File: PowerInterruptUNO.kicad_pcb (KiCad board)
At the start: 2 copper layers, 68.6 x 53.3 mm, 8 parts, among them J1 Power, J2 Digital/PWM, J3 Analog, J4 Digital/PWM

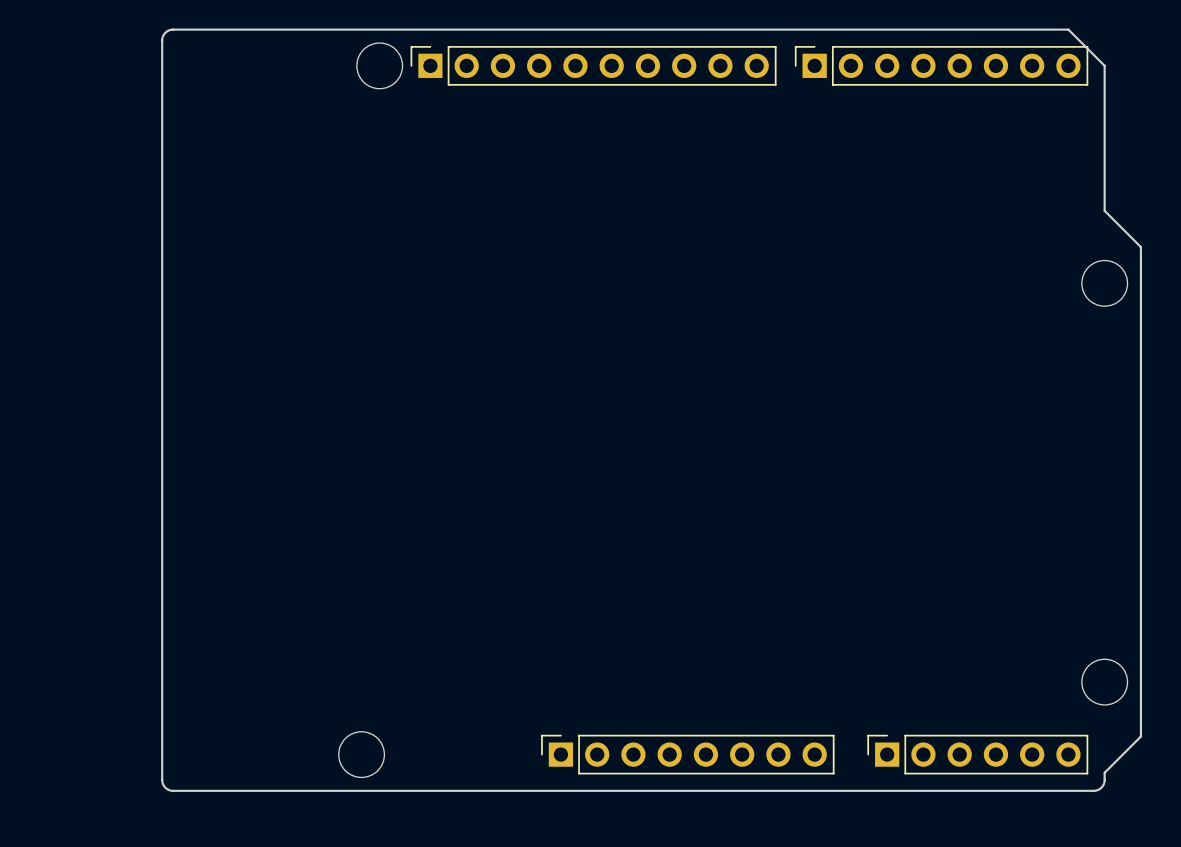
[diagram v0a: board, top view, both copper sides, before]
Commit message: Place parts on PCB.
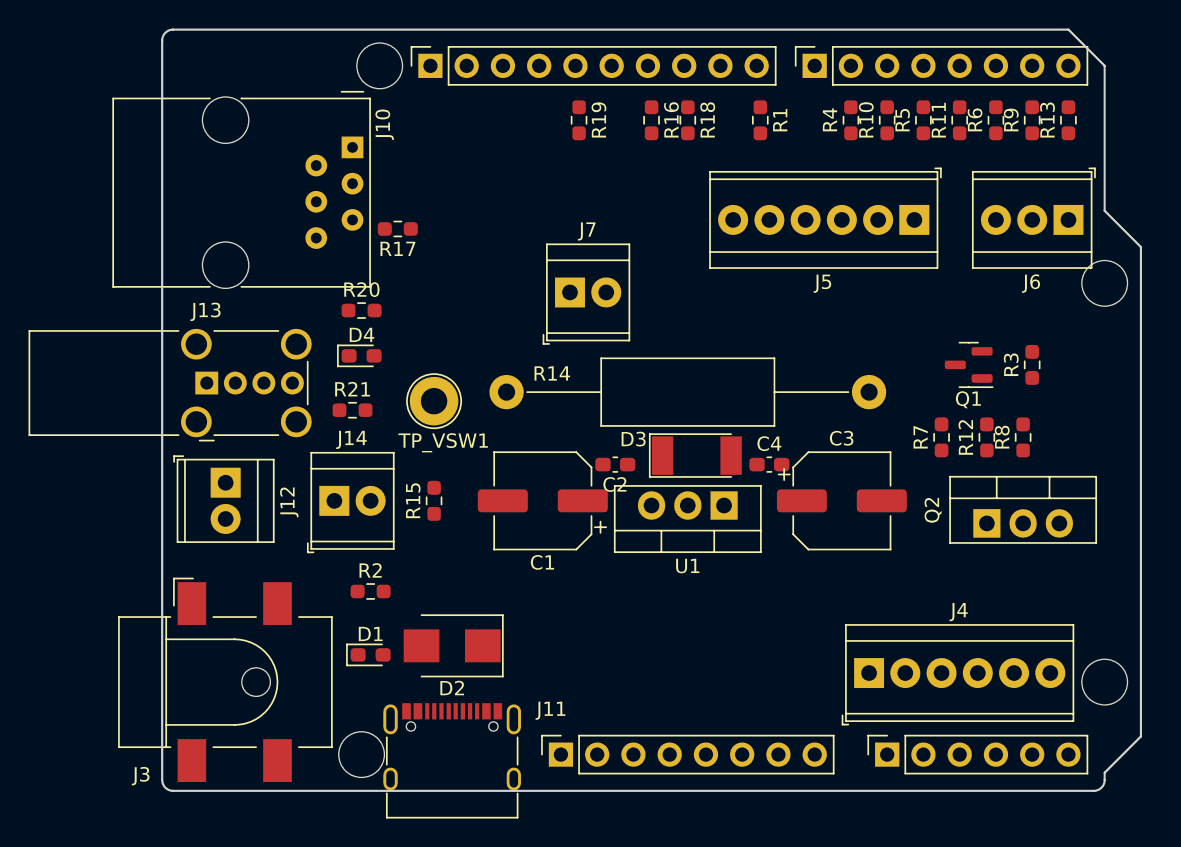
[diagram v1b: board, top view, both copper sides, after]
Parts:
- added C1: 47uF 25V, Capacitor_SMD:CP_Elec_6.3x5.3, F.Cu at (126.7, 79.7)
- added C2: 100nF 50V, Capacitor_SMD:C_0603_1608Metric_Pad1.08x0.95mm_HandSolder, F.Cu at (131.8, 77.1)
- added C3: 47uF 25V, Capacitor_SMD:CP_Elec_6.3x5.3, F.Cu at (147.6, 79.7)
- added C4: 100nF 50V, Capacitor_SMD:C_0603_1608Metric_Pad1.08x0.95mm_HandSolder, F.Cu at (142.5, 77.1)
- added D1: LD271, LED_SMD:LED_0603_1608Metric_Pad1.05x0.95mm_HandSolder, F.Cu at (114.6, 90.5)
- added D2: Schottky 2A, Diode_SMD:D_SMB, F.Cu at (120.3, 89.8)
- added D3: SM4001, Diode_SMD:D_MELF, F.Cu at (137.5, 76.5)
- added D4: LD271, LED_SMD:LED_0603_1608Metric_Pad1.05x0.95mm_HandSolder, F.Cu at (114.0, 69.5)
- added J10: 6P6C, Connector_RJ:RJ12_Amphenol_54601, F.Cu at (113.3, 54.9)
- added J11: USB_C_Receptacle_USB2.0, Connector_USB:USB_C_Receptacle_XKB_U262-16XN-4BVC11, F.Cu at (120.3, 98.1)
- added J12: Screw_Terminal_01x02, TerminalBlock_TE-Connectivity:TerminalBlock_TE_282834-2_1x02_P2.54mm_Horizontal, F.Cu at (104.4, 78.4)
- added J13: USB_A_Vertical, Connector_USB:USB_A_Wuerth_614004134726_Horizontal, F.Cu at (103.1, 71.4)
- added J14: Screw_Terminal_01x02, TerminalBlock_TE-Connectivity:TerminalBlock_TE_282834-2_1x02_P2.54mm_Horizontal, F.Cu at (112.1, 79.7)
- added J3: Barrel_Jack_Switch_SMT, Connector_BarrelJack:BarrelJack_CLIFF_FC681465S_SMT_Horizontal, F.Cu at (105.1, 92.4)
- added J4: Screw_Terminal_01x06, TerminalBlock_TE-Connectivity:TerminalBlock_TE_282834-6_1x06_P2.54mm_Horizontal, F.Cu at (149.5, 91.7)
- added J5: Screw_Terminal_01x06, TerminalBlock_TE-Connectivity:TerminalBlock_TE_282834-6_1x06_P2.54mm_Horizontal, F.Cu at (152.7, 60.0)
- added J6: Screw_Terminal_01x03, TerminalBlock_TE-Connectivity:TerminalBlock_TE_282834-3_1x03_P2.54mm_Horizontal, F.Cu at (163.5, 60.0)
- added J7: Screw_Terminal_01x02, TerminalBlock_TE-Connectivity:TerminalBlock_TE_282834-2_1x02_P2.54mm_Horizontal, F.Cu at (128.6, 65.1)
- added Q1: MMBT3904, Package_TO_SOT_SMD:SOT-23, F.Cu at (156.5, 70.2)
- added Q2: TIP42, Package_TO_SOT_THT:TO-220-3_Vertical, F.Cu at (157.8, 81.3)
- added R1: 1K, Resistor_SMD:R_0603_1608Metric_Pad0.98x0.95mm_HandSolder, F.Cu at (141.9, 53.0)
- added R10: 1K, Resistor_SMD:R_0603_1608Metric_Pad0.98x0.95mm_HandSolder, F.Cu at (150.8, 53.0)
- added R11: 1K, Resistor_SMD:R_0603_1608Metric_Pad0.98x0.95mm_HandSolder, F.Cu at (155.9, 53.0)
- added R12: 1K, Resistor_SMD:R_0603_1608Metric_Pad0.98x0.95mm_HandSolder, F.Cu at (157.8, 75.2)
- added R13: 1K, Resistor_SMD:R_0603_1608Metric_Pad0.98x0.95mm_HandSolder, F.Cu at (163.5, 53.0)
- added R14: 12R, 1/2W, Resistor_THT:R_Axial_DIN0414_L11.9mm_D4.5mm_P25.40mm_Horizontal, F.Cu at (124.1, 72.1)
- added R15: 1R, Resistor_SMD:R_0603_1608Metric_Pad0.98x0.95mm_HandSolder, F.Cu at (119.0, 79.7)
- added R16: 330, Resistor_SMD:R_0603_1608Metric_Pad0.98x0.95mm_HandSolder, F.Cu at (134.3, 53.0)
- added R17: 330, Resistor_SMD:R_0603_1608Metric_Pad0.98x0.95mm_HandSolder, F.Cu at (116.5, 60.6)
- added R18: 330, Resistor_SMD:R_0603_1608Metric_Pad0.98x0.95mm_HandSolder, F.Cu at (136.8, 53.0)
- added R19: 330, Resistor_SMD:R_0603_1608Metric_Pad0.98x0.95mm_HandSolder, F.Cu at (129.2, 53.0)
- added R2: 330, Resistor_SMD:R_0603_1608Metric_Pad0.98x0.95mm_HandSolder, F.Cu at (114.6, 86.0)
- added R20: 330, Resistor_SMD:R_0603_1608Metric_Pad0.98x0.95mm_HandSolder, F.Cu at (114.0, 66.3)
- added R21: ZERO, Resistor_SMD:R_0603_1608Metric_Pad0.98x0.95mm_HandSolder, F.Cu at (113.3, 73.3)
- added R3: 10K, Resistor_SMD:R_0603_1608Metric_Pad0.98x0.95mm_HandSolder, F.Cu at (161.0, 70.2)
- added R4: 1K, Resistor_SMD:R_0603_1608Metric_Pad0.98x0.95mm_HandSolder, F.Cu at (148.3, 53.0)
- added R5: 1K, Resistor_SMD:R_0603_1608Metric_Pad0.98x0.95mm_HandSolder, F.Cu at (153.3, 53.0)
- added R6: 1K, Resistor_SMD:R_0603_1608Metric_Pad0.98x0.95mm_HandSolder, F.Cu at (158.4, 53.0)
- added R7: 1K, Resistor_SMD:R_0603_1608Metric_Pad0.98x0.95mm_HandSolder, F.Cu at (154.6, 75.2)
- added R8: 10K, Resistor_SMD:R_0603_1608Metric_Pad0.98x0.95mm_HandSolder, F.Cu at (160.3, 75.2)
- added R9: 1K, Resistor_SMD:R_0603_1608Metric_Pad0.98x0.95mm_HandSolder, F.Cu at (161.0, 53.0)
- added TP_VSW1: TestPoint, TestPoint:TestPoint_Loop_D2.50mm_Drill1.85mm, F.Cu at (119.0, 72.7)
- added U1: LM317_TO-220, Package_TO_SOT_THT:TO-220-3_Vertical, F.Cu at (139.4, 80.0)
- renumbered J3 to J2, J2 to J8, J4 to J9
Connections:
- J1 pad 4: +3V3 -> unconnected-(J1-Pad4)
- J1 pad 5: +5V -> unconnected-(J1-Pad5)
- J1 pad 8: VCC -> unconnected-(J1-Pad8)
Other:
- board text added: "PowerInterruptUNO Amused Scientist 20220714"

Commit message: Initial routing. 100% connected but lots of DRC errors to track down.
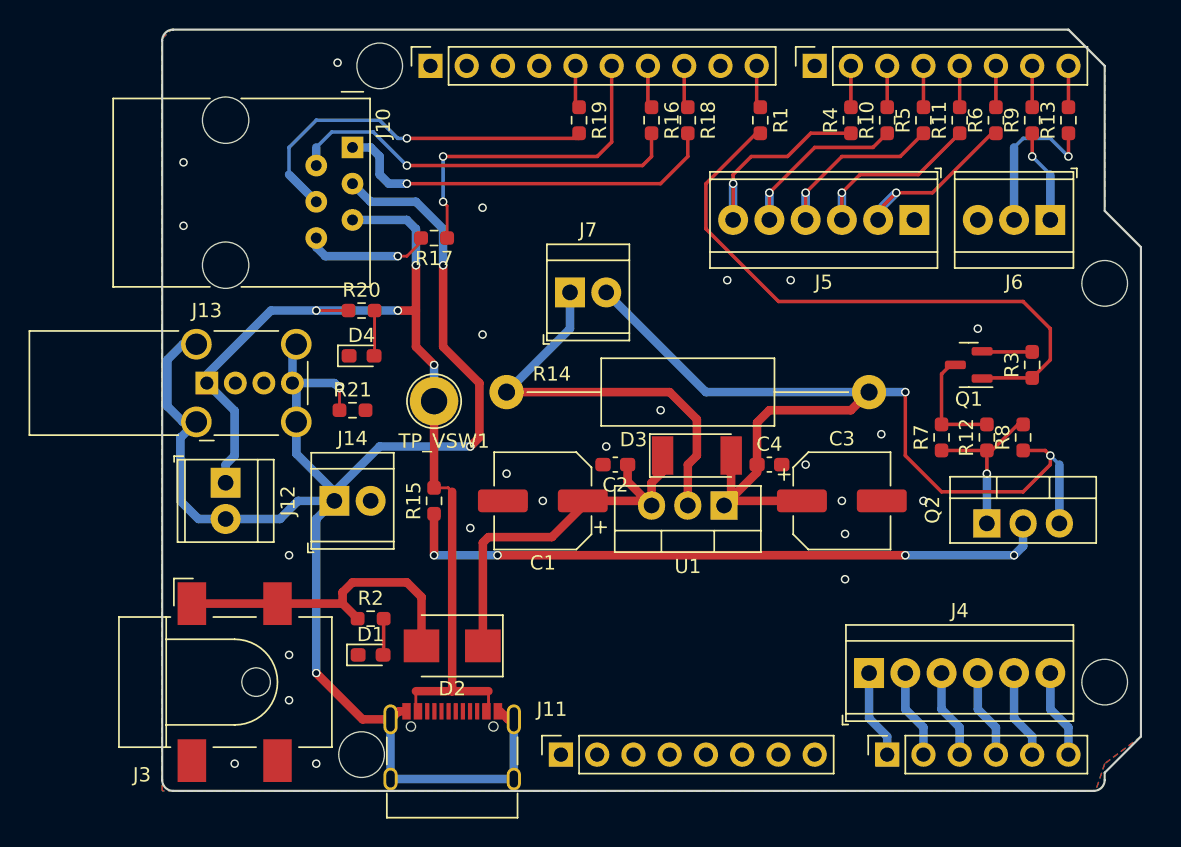
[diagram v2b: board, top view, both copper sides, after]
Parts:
- moved R17 2.62 mm to (119.0, 61.3)
- moved R2 1.91 mm to (114.6, 87.9)
- moved J6 1.27 mm to (162.2, 60.0)
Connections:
- J8 pad 1: /SCL/A5 -> unconnected-(J8-Pad1)
- J8 pad 2: /SDA/A4 -> unconnected-(J8-Pad2)
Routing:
- net Net-(J10-Pad3): track 0.00 -> 117.0 mm, vias 0 -> 4
- net +VSW: track 0.00 -> 74.1 mm, vias 0 -> 4
- net VCC: track 0.00 -> 72.8 mm, vias 0 -> 2
- net Net-(Q2-Pad2): track 0.00 -> 46.0 mm, vias 0 -> 4
- net Net-(Q1-Pad1): track 0.00 -> 43.0 mm
- net Net-(J7-Pad1): track 0.00 -> 29.3 mm
- net Net-(J10-Pad2): track 0.00 -> 28.1 mm, vias 0 -> 1
- net Net-(C1-Pad1): track 0.00 -> 28.0 mm
- net Net-(J10-Pad1): track 0.00 -> 27.7 mm, vias 0 -> 1
- net Net-(J10-Pad4): track 0.00 -> 26.6 mm, vias 0 -> 1
- net /12: track 0.00 -> 23.4 mm, vias 0 -> 2
- net +9V: track 0.00 -> 22.5 mm
- net Net-(J5-Pad6): track 0.00 -> 15.2 mm, vias 0 -> 1
- net Net-(J5-Pad5): track 0.00 -> 13.8 mm, vias 0 -> 1
- net Net-(J5-Pad4): track 0.00 -> 13.8 mm, vias 0 -> 1
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- added copper zone on B.Cu, net GND
- added copper zone on F.Cu, net GND
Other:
- board text added: "JLCJLCJLCJLC"

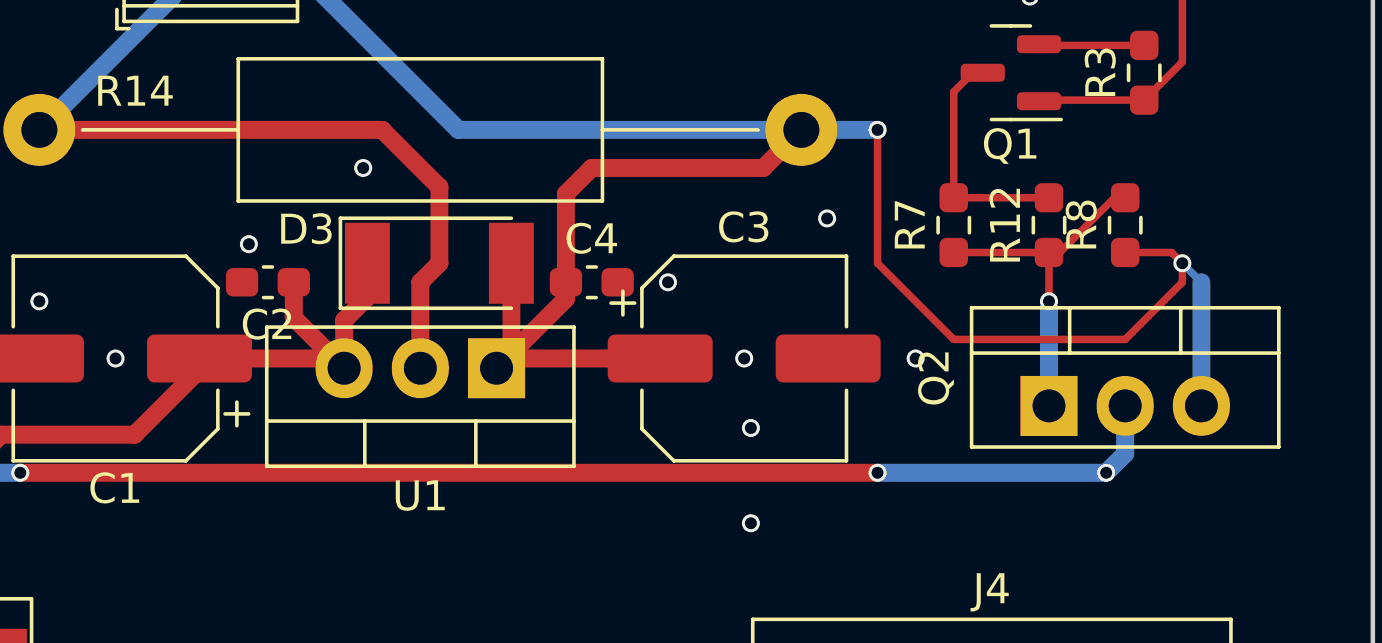
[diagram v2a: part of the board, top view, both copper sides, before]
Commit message: Clear some DRC errors but many remaining including Silkscreen clipping solder mask.
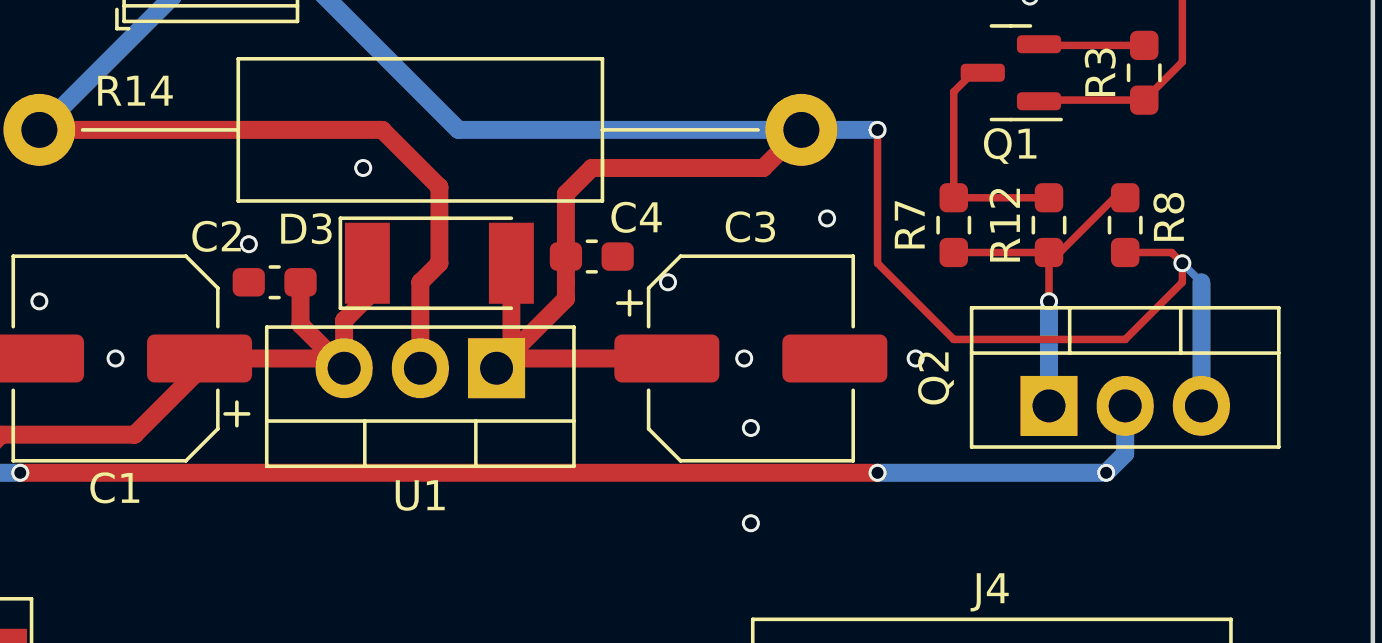
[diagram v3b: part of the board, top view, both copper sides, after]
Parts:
- moved C4 0.86 mm to (142.5, 76.3)
- moved C2 0.22 mm to (132.0, 77.1)
- moved C3 0.22 mm to (147.8, 79.7)
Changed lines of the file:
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@@
   )
   (footprint "Capacitor_SMD:C_0603_1608Metric_Pad1.08x0.95mm_HandSolder" (layer "F.Cu")
-    (at 142.545 77.14)
+    (at 142.545 76.281815)
     (descr "Capacitor SMD 0603 (1608 Metric), square (rectangular) end terminal, IPC_7351 nominal with elongated pad for handsoldering. (Body size source: IPC-SM-782 page 76, https://www.pcb-3d.com/wordpress/wp-content/uploads/ipc-sm-782a_amendment_1_and_2.pdf), generated with kicad-footprint-generator")
     (tags "capacitor handsolder")
@@
     (property "Sheetname" "")
     (attr smd)
-    (fp_text reference "C4" (at 0 -1.43) (layer "F.SilkS")
+    (fp_text reference "C4" (at 1.493185 -1.27) (layer "F.SilkS")
       (effects (font (size 1 1) (thickness 0.15)))
     )
@@
     (property "Sheetname" "")
     (attr smd)
-    (fp_text reference "R8" (at 0 -1.43 90) (layer "F.SilkS")
+    (fp_text reference "R8" (at 0.254724 1.493185 90) (layer "F.SilkS")
       (effects (font (size 1 1) (thickness 0.15)))
     )
@@
   )
   (footprint "Capacitor_SMD:C_0603_1608Metric_Pad1.08x0.95mm_HandSolder" (layer "F.Cu")
-    (at 131.75 77.14 180)
+    (at 131.973185 77.14 180)
     (descr "Capacitor SMD 0603 (1608 Metric), square (rectangular) end terminal, IPC_7351 nominal with elongated pad for handsoldering. (Body size source: IPC-SM-782 page 76, https://www.pcb-3d.com/wordpress/wp-content/uploads/ipc-sm-782a_amendment_1_and_2.pdf), generated with kicad-footprint-generator")
     (tags "capacitor handsolder")
@@
     (property "Sheetname" "")
     (attr smd)
-    (fp_text reference "C2" (at 0 -1.43) (layer "F.SilkS")
+    (fp_text reference "C2" (at 1.905 1.493185) (layer "F.SilkS")
       (effects (font (size 1 1) (thickness 0.15)))
     )
@@
   )
   (footprint "Capacitor_SMD:CP_Elec_6.3x5.3" (layer "F.Cu")
-    (at 147.625 79.68)
+    (at 147.848185 79.68)
     (descr "SMD capacitor, aluminum electrolytic, Cornell Dubilier, 6.3x5.3mm")
     (tags "capacitor electrolytic")
@@
   (via (at 101.493185 55.961815) (size 0.6) (drill 0.4) (layers "F.Cu" "B.Cu") (free) (net 1))
   (via (at 157.15 67.615) (size 0.6) (drill 0.4) (layers "F.Cu" "B.Cu") (free) (net 1))
+  (segment (start 132.8575 78.5725) (end 132.835685 78.550685) (width 0.6) (layer "F.Cu") (net 3))
   (segment (start 134.29 78.41) (end 134.29 80.005) (width 0.6) (layer "F.Cu") (net 3))
-  (segment (start 132.6125 77.14) (end 132.6125 78.3275) (width 0.6) (layer "F.Cu") (net 3))
   (segment (start 129.47 80.055) (end 129.47 79.68) (width 0.6) (layer "F.Cu") (net 3))
   (segment (start 122.86 82.22) (end 127.305 82.22) (width 0.6) (layer "F.Cu") (net 3))
   (segment (start 129.47 79.68) (end 133.965 79.68) (width 0.6) (layer "F.Cu") (net 3))
-  (segment (start 132.6125 78.3275) (end 134.29 80.005) (width 0.6) (layer "F.Cu") (net 3))
+  (segment (start 134.29 80.005) (end 132.8575 78.5725) (width 0.6) (layer "F.Cu") (net 3))
+  (segment (start 132.835685 78.550685) (end 132.835685 77.14) (width 0.6) (layer "F.Cu") (net 3))
   (segment (start 135.065 76.505) (end 135.065 77.635) (width 0.6) (layer "F.Cu") (net 3))
   (segment (start 127.305 82.22) (end 129.47 80.055) (width 0.6) (layer "F.Cu") (net 3))
